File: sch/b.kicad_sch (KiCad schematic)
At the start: 1 part

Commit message: Update
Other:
- moved on the sheet: C?
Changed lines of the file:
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@@
 (kicad_sch (version 20211123) (generator eeschema)
   (paper "A4")
-  (symbol (lib_id "Device:C") (at 138.43 97.79 0) (unit 1)
+  (symbol (lib_id "Device:C") (at 135.89 97.79 0) (unit 1)
     (in_bom yes) (on_board yes) (fields_autoplaced)
-    (property "Reference" "C?" (id 0) (at 142.24 96.5199 0)
+    (property "Reference" "C?" (id 0) (at 139.7 96.5199 0)
       (effects (font (size 1.27 1.27)) (justify left))
     )
-    (property "Value" "C" (id 1) (at 142.24 99.0599 0)
+    (property "Value" "C" (id 1) (at 139.7 99.0599 0)
       (effects (font (size 1.27 1.27)) (justify left))
     )
-    (property "Footprint" "" (id 2) (at 139.3952 101.6 0)
+    (property "Footprint" "" (id 2) (at 136.8552 101.6 0)
       (effects (font (size 1.27 1.27)) hide)
     )
-    (property "Datasheet" "~" (id 3) (at 138.43 97.79 0)
+    (property "Datasheet" "~" (id 3) (at 135.89 97.79 0)
       (effects (font (size 1.27 1.27)) hide)
     )
@@
     (pin "2")
   )
-  (sheet (at 162.56 99.06) (size 36.83 16.51) (fields_autoplaced)
+  (sheet (at 148.59 88.9) (size 36.83 16.51) (fields_autoplaced)
     (stroke (width 0.1524) (type solid) (color 0 0 0 0))
     (fill (color 0 0 0 0.0000))
-    (property "Sheet name" "C" (id 0) (at 162.56 98.3484 0)
+    (property "Sheet name" "C" (id 0) (at 148.59 88.1884 0)
       (effects (font (size 1.27 1.27)) (justify left bottom))
     )
-    (property "Sheet file" "c.kicad_sch" (id 1) (at 162.56 116.1546 0)
+    (property "Sheet file" "c.kicad_sch" (id 1) (at 148.59 105.9946 0)
       (effects (font (size 1.27 1.27)) (justify left top))
     )

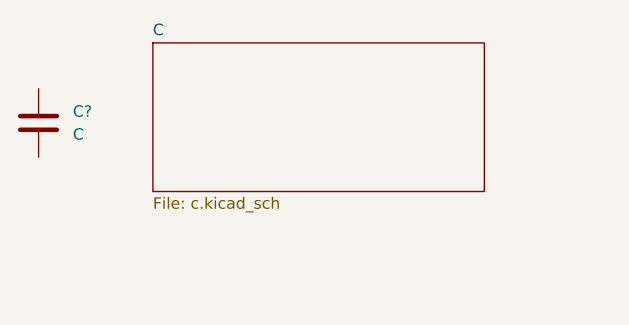
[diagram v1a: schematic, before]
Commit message: Add file and sheet instance with spaces. Anotate parts.
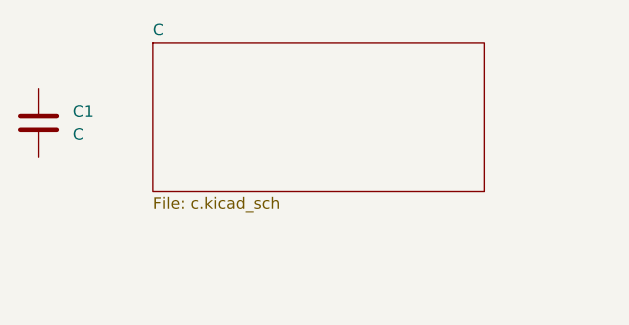
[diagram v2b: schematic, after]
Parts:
- gave numbers to parts that had none: 1
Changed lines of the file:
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@@
   (symbol (lib_id "Device:C") (at 135.89 97.79 0) (unit 1)
     (in_bom yes) (on_board yes) (fields_autoplaced)
-    (property "Reference" "C?" (id 0) (at 139.7 96.5199 0)
+    (property "Reference" "C1" (id 0) (at 139.7 96.5199 0)
       (effects (font (size 1.27 1.27)) (justify left))
     )
